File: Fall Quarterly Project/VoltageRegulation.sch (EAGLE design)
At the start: 19 parts

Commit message: Update 1.2
Introduced part of the voltage sense circuitry, filter, and amplifier. most parts still need values though, those of you with r or c values can feel free to label them.
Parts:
- removed C2: (no value), rcl:C-US050-055X075
- removed D2: (no value), diode:DIODE-DO07
- removed IC1: (no value), v-reg:78XXS
- removed VIN: (no value), con-wago-500:W237-102
- added IC3: L272M, linear:L272M
- added R1: 30k, rcl:R-US_0207/7
- added R2, R3: 10k, rcl:R-US_0207/7
- added R4: (no value), rcl:R-US_0411/12
- C1: device rcl:C-US050-055X075 -> rcl:C-US050-024X044
- D1: value (none) -> SB320; device diode:DIODE-DO07 -> diode:SB320
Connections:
- new net N$2: IC3A.OUT, IC3B.+IN, R1.2, R4.1
- new net N$4: IC3A.-IN, R1.1, R2.1
- new net N$5: C1.1, IC3A.+IN, R3.2
- new net N$6: IC3B.-IN, R4.2
- net +12V: now also IC3P.V+; no longer C1.1, D2.C, IC1.IN
- net +5V: no longer C2.1, IC1.OUT
- net 10SDIGIT5: now also U$1.D12; no longer U$1.D11
- net GND: now also IC3P.GND, R2.2; no longer C2.2, IC1.GND, VIN-2.KL
- net N$1: now also R3.1, U$1.D11; no longer D1.A, VIN-1.KL
- net N$3: now also D1.A; no longer D2.A

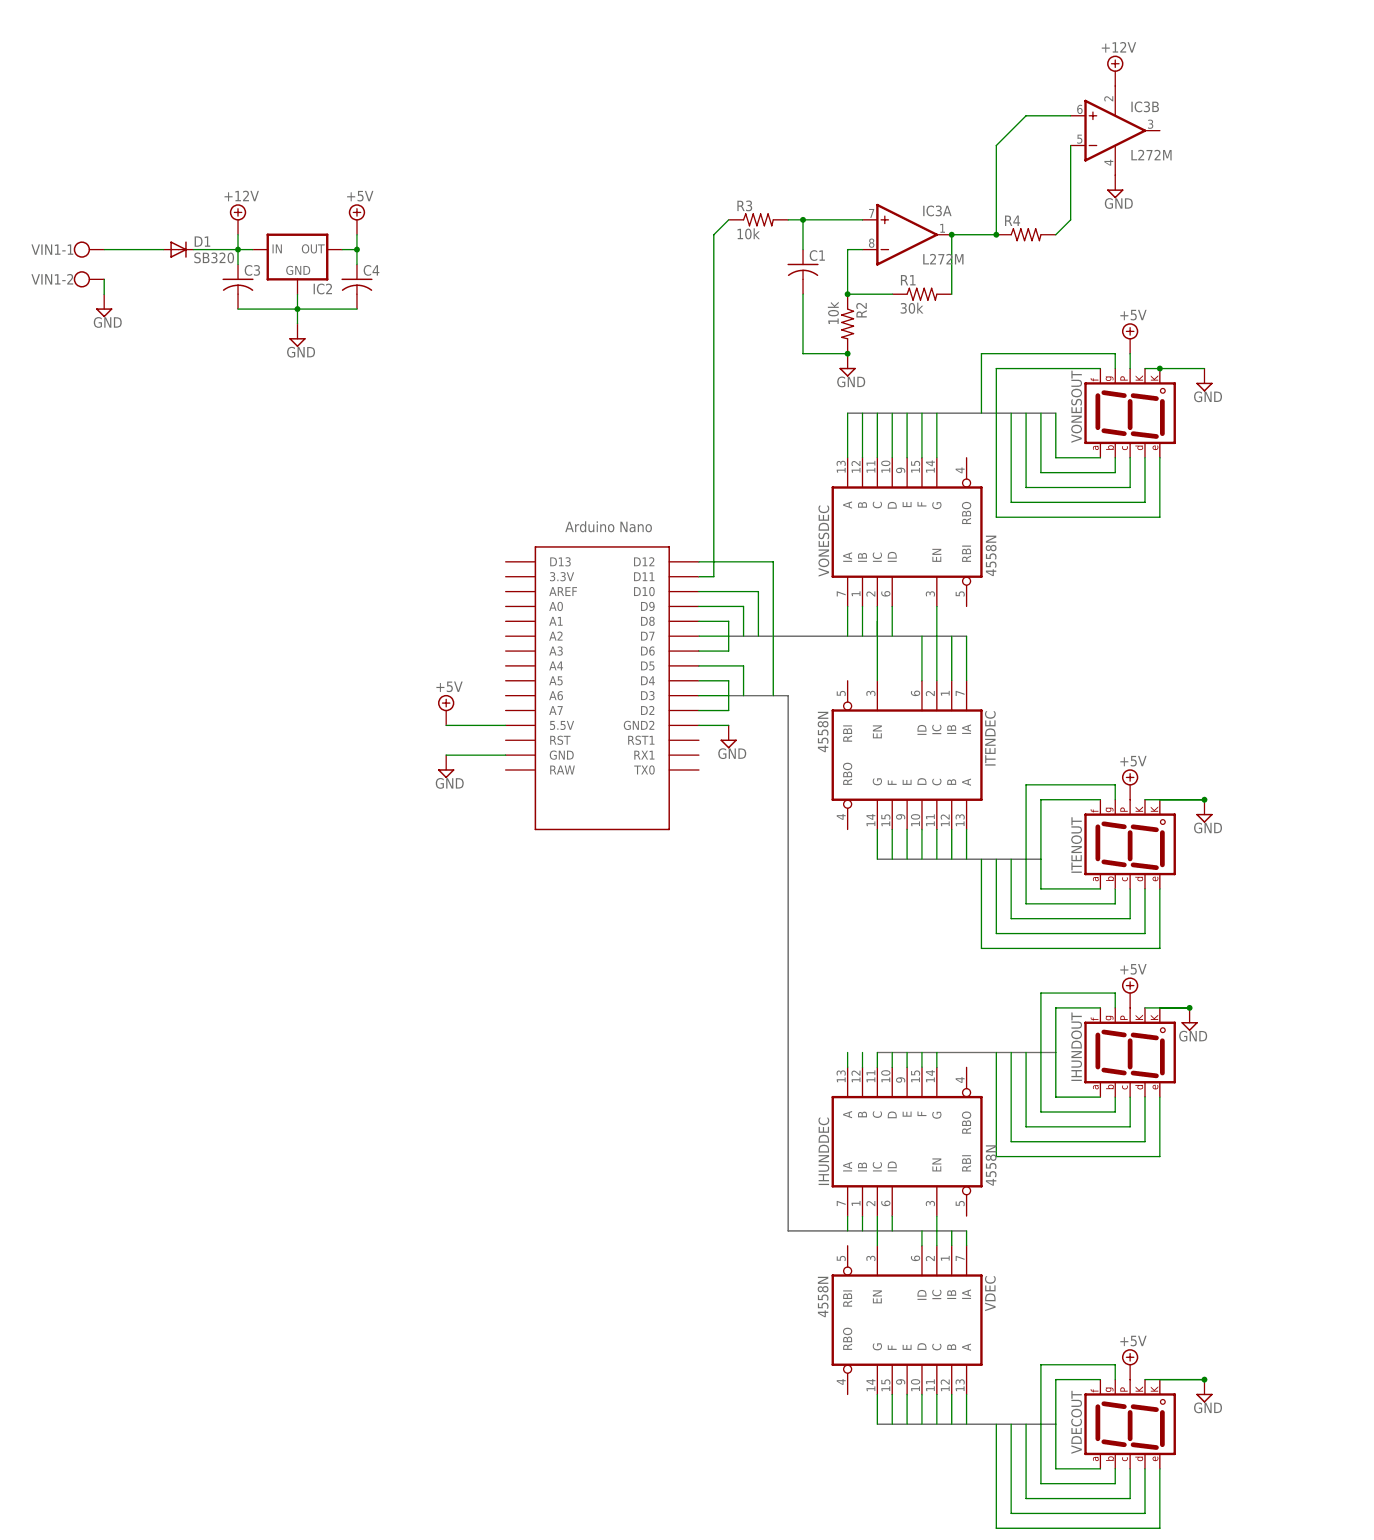
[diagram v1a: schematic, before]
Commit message: Update 1.3
All major parts have now been included in the schematic, only adjustments need to be made now. I know some resistor values have been implemented with series or parallel combinations in order use stockroom parts, and this is not accounted for. Values still need to be added to parts for the bill of materials as well as the silkscreening process. I've tried laying some traces as well in the board layout, but the config i've been trying out seems bad and needs an entire rework. We are at the point that board layout and tracing can commence.
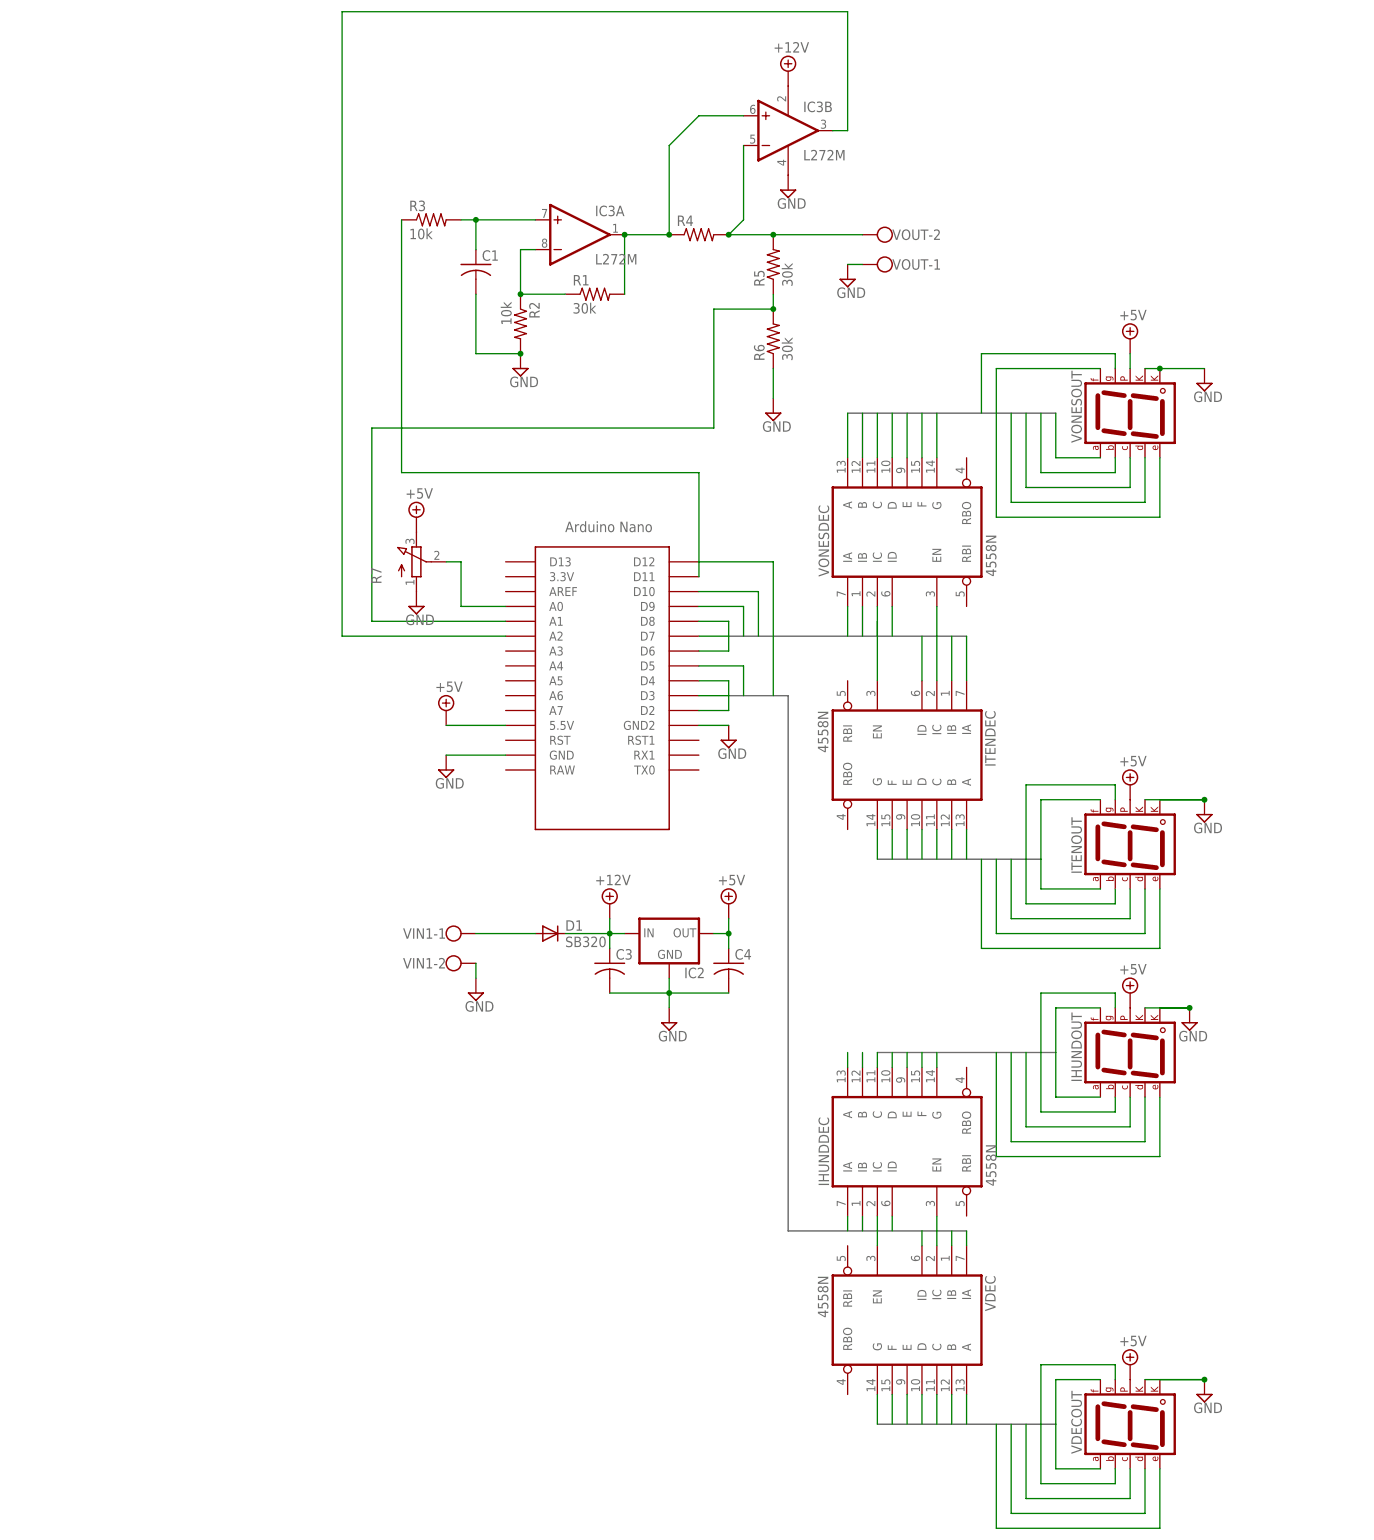
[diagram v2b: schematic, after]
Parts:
- added R5, R6: 30k, rcl:R-US_0207/7
- added R7: (no value), pot:3RP/1610N
- added VOUT: (no value), con-wago-500:W237-102
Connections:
- new net N$10: IC3B.OUT, U$1.A2
- new net N$7: R5.1, R6.2, U$1.A1
- new net N$9: R7.S, U$1.A0
- net +5V: now also R7.E
- net GND: now also R6.1, R7.A, VOUT-1.KL
- net N$6: now also R5.2, VOUT-2.KL
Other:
- moved on the sheet: C1, C3, C4, D1, IC2, IC3A, IC3B, R1, R2, R3, R4, VIN1-1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

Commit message: Update 1.4
Just began routing the board and deciding where parts will lie. I'm keeping to one layer of the board for now, that way any nets that need to be escaped to another side of the board won't need any crazy routing to reach their destination.
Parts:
- removed D1: SB320, diode:SB320
- added D2: 1N4004, diode:1N4004
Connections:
- net +12V: now also D2.C; no longer D1.C
- net +5V: now also IHUNDDECP.VSS, ITENDECP.VSS, VDECP.VSS, VONESDECP.VSS
- net 10SDIGIT5: no longer ITENDECA.EN
- net 1SDIGIT5: now also ITENDECA.EN
- net GND: now also IHUNDDECP.VDD, ITENDECP.VDD, VDECP.VDD, VONESDECP.VDD
- net N$3: now also D2.A; no longer D1.A
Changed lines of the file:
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@@
 <part name="R3" library="rcl" library_urn="urn:adsk.eagle:library:334" deviceset="R-US_" device="0207/7" package3d_urn="urn:adsk.eagle:package:23493/1" value="10k"/>
 <part name="C1" library="rcl" library_urn="urn:adsk.eagle:library:334" deviceset="C-US" device="050-024X044" package3d_urn="urn:adsk.eagle:package:23643/1"/>
-<part name="D1" library="diode" library_urn="urn:adsk.eagle:library:210" deviceset="SB320" device="" package3d_urn="urn:adsk.eagle:package:43365/1"/>
 <part name="R4" library="rcl" library_urn="urn:adsk.eagle:library:334" deviceset="R-US_" device="0411/12" package3d_urn="urn:adsk.eagle:package:23578/1"/>
 <part name="R5" library="rcl" library_urn="urn:adsk.eagle:library:334" deviceset="R-US_" device="0207/7" package3d_urn="urn:adsk.eagle:package:23493/1" value="30k">
@@
 <part name="VOUT" library="con-wago-500" library_urn="urn:adsk.eagle:library:195" deviceset="W237-102" device="" package3d_urn="urn:adsk.eagle:package:10688/1"/>
 <part name="SUPPLY22" library="supply2" library_urn="urn:adsk.eagle:library:372" deviceset="GND" device=""/>
+<part name="SUPPLY23" library="supply2" library_urn="urn:adsk.eagle:library:372" deviceset="+5V" device=""/>
+<part name="SUPPLY24" library="supply2" library_urn="urn:adsk.eagle:library:372" deviceset="+5V" device=""/>
+<part name="SUPPLY25" library="supply2" library_urn="urn:adsk.eagle:library:372" deviceset="+5V" device=""/>
+<part name="SUPPLY26" library="supply2" library_urn="urn:adsk.eagle:library:372" deviceset="+5V" device=""/>
+<part name="SUPPLY27" library="supply2" library_urn="urn:adsk.eagle:library:372" deviceset="GND" device=""/>
+<part name="SUPPLY28" library="supply2" library_urn="urn:adsk.eagle:library:372" deviceset="GND" device=""/>
+<part name="SUPPLY29" library="supply2" library_urn="urn:adsk.eagle:library:372" deviceset="GND" device=""/>
+<part name="SUPPLY30" library="supply2" library_urn="urn:adsk.eagle:library:372" deviceset="GND" device=""/>
+<part name="D2" library="diode" library_urn="urn:adsk.eagle:library:210" deviceset="1N4004" device="" package3d_urn="urn:adsk.eagle:package:43336/1"/>
 </parts>
 <sheets>
@@
 <instance part="R3" gate="G$1" x="-78.74" y="170.18"/>
 <instance part="C1" gate="G$1" x="-71.12" y="162.56"/>
-<instance part="D1" gate="1" x="-58.42" y="48.26"/>
 <instance part="R4" gate="G$1" x="-33.02" y="167.64"/>
 <instance part="R5" gate="G$1" x="-20.32" y="162.56" rot="R90">
@@
 <attribute name="R" x="-20.32" y="149.86" size="1.778" layer="96" rot="R90" display="off"/>
 </instance>
-<instance part="SUPPLY5" gate="GND" x="-20.32" y="137.16"/>
+<instance part="SUPPLY5" gate="GND" x="-20.32" y="142.24"/>
 <instance part="R7" gate="G$1" x="-81.28" y="111.76"/>
 <instance part="SUPPLY20" gate="+5V" x="-81.28" y="119.38"/>
@@
 <instance part="VOUT" gate="-2" x="0" y="167.64" rot="R180"/>
 <instance part="SUPPLY22" gate="GND" x="-7.62" y="160.02"/>
+<instance part="VONESDEC" gate="P" x="50.8" y="101.6" rot="R180"/>
+<instance part="ITENDEC" gate="P" x="76.2" y="101.6" rot="R180"/>
+<instance part="IHUNDDEC" gate="P" x="58.42" y="101.6" rot="R180"/>
+<instance part="VDEC" gate="P" x="68.58" y="101.6" rot="R180"/>
+<instance part="SUPPLY23" gate="+5V" x="58.42" y="114.3"/>
+<instance part="SUPPLY24" gate="+5V" x="50.8" y="114.3"/>
+<instance part="SUPPLY25" gate="+5V" x="68.58" y="114.3"/>
+<instance part="SUPPLY26" gate="+5V" x="76.2" y="114.3"/>
+<instance part="SUPPLY27" gate="GND" x="50.8" y="88.9"/>
+<instance part="SUPPLY28" gate="GND" x="58.42" y="88.9"/>
+<instance part="SUPPLY29" gate="GND" x="68.58" y="88.9"/>
+<instance part="SUPPLY30" gate="GND" x="76.2" y="88.9"/>
+<instance part="D2" gate="1" x="-58.42" y="48.26"/>
 </instances>
 <busses>
@@
 <bus name="4DIGIT[1..7]">
 <segment>
-<wire x1="27.94" y1="27.94" x2="-2.54" y2="27.94" width="0.762" layer="92"/>
+<wire x1="27.94" y1="27.94" x2="-7.62" y2="27.94" width="0.762" layer="92"/>
 </segment>
 </bus>
@@
 <net name="1SDIGIT3" class="0">
 <segment>
-<pinref part="VONESDEC" gate="A" pin="IC"/>
-<wire x1="-2.54" y1="99.06" x2="-2.54" y2="104.14" width="0.1524" layer="91"/>
-</segment>
-<segment>
 <pinref part="ITENDEC" gate="A" pin="IC"/>
 <wire x1="7.62" y1="99.06" x2="7.62" y2="91.44" width="0.1524" layer="91"/>
@@
 <pinref part="U$1" gate="G$1" pin="D8"/>
 <wire x1="-27.94" y1="101.6" x2="-33.02" y2="101.6" width="0.1524" layer="91"/>
+</segment>
+<segment>
+<pinref part="VONESDEC" gate="A" pin="IC"/>
+<wire x1="-2.54" y1="104.14" x2="-2.54" y2="99.06" width="0.1524" layer="91"/>
 </segment>
 </net>
@@
 <net name="4DIGIT1" class="0">
 <segment>
-<pinref part="IHUNDDEC" gate="A" pin="A"/>
-<wire x1="-7.62" y1="25.4" x2="-7.62" y2="27.94" width="0.1524" layer="91"/>
-</segment>
-<segment>
 <pinref part="IHUNDOUT" gate="G$1" pin="A"/>
 <wire x1="27.94" y1="20.32" x2="35.56" y2="20.32" width="0.1524" layer="91"/>
 <wire x1="27.94" y1="20.32" x2="27.94" y2="27.94" width="0.1524" layer="91"/>
 </segment>
+<segment>
+<pinref part="IHUNDDEC" gate="A" pin="A"/>
+<wire x1="-7.62" y1="27.94" x2="-7.62" y2="25.4" width="0.1524" layer="91"/>
+</segment>
 </net>
 <net name="4DIGIT2" class="0">
-<segment>
-<pinref part="IHUNDDEC" gate="A" pin="B"/>
-<wire x1="-5.08" y1="25.4" x2="-5.08" y2="27.94" width="0.1524" layer="91"/>
-</segment>
 <segment>
 <pinref part="IHUNDOUT" gate="G$1" pin="B"/>
@@
 <wire x1="38.1" y1="17.78" x2="25.4" y2="17.78" width="0.1524" layer="91"/>
 <wire x1="25.4" y1="17.78" x2="25.4" y2="27.94" width="0.1524" layer="91"/>
+</segment>
+<segment>
+<pinref part="IHUNDDEC" gate="A" pin="B"/>
+<wire x1="-5.08" y1="27.94" x2="-5.08" y2="25.4" width="0.1524" layer="91"/>
 </segment>
 </net>
@@
 <pinref part="SUPPLY20" gate="+5V" pin="+5V"/>
 <pinref part="R7" gate="G$1" pin="E"/>
+</segment>
+<segment>
+<pinref part="VONESDEC" gate="P" pin="VSS"/>
+<pinref part="SUPPLY24" gate="+5V" pin="+5V"/>
+<wire x1="50.8" y1="109.22" x2="50.8" y2="111.76" width="0.1524" layer="91"/>
+</segment>
+<segment>
+<pinref part="IHUNDDEC" gate="P" pin="VSS"/>
+<pinref part="SUPPLY23" gate="+5V" pin="+5V"/>
+<wire x1="58.42" y1="109.22" x2="58.42" y2="111.76" width="0.1524" layer="91"/>
+</segment>
+<segment>
+<pinref part="SUPPLY25" gate="+5V" pin="+5V"/>
+<pinref part="VDEC" gate="P" pin="VSS"/>
+<wire x1="68.58" y1="111.76" x2="68.58" y2="109.22" width="0.1524" layer="91"/>
+</segment>
+<segment>
+<pinref part="ITENDEC" gate="P" pin="VSS"/>
+<pinref part="SUPPLY26" gate="+5V" pin="+5V"/>
+<wire x1="76.2" y1="109.22" x2="76.2" y2="111.76" width="0.1524" layer="91"/>
 </segment>
 </net>
@@
 <pinref part="SUPPLY5" gate="GND" pin="GND"/>
 <pinref part="R6" gate="G$1" pin="1"/>
-<wire x1="-20.32" y1="139.7" x2="-20.32" y2="144.78" width="0.1524" layer="91"/>
 </segment>
 <segment>
@@
 <wire x1="-5.08" y1="162.56" x2="-7.62" y2="162.56" width="0.1524" layer="91"/>
 </segment>
+<segment>
+<pinref part="VONESDEC" gate="P" pin="VDD"/>
+<pinref part="SUPPLY27" gate="GND" pin="GND"/>
+<wire x1="50.8" y1="93.98" x2="50.8" y2="91.44" width="0.1524" layer="91"/>
+</segment>
+<segment>
+<pinref part="SUPPLY28" gate="GND" pin="GND"/>
+<pinref part="IHUNDDEC" gate="P" pin="VDD"/>
+<wire x1="58.42" y1="91.44" x2="58.42" y2="93.98" width="0.1524" layer="91"/>
+</segment>
+<segment>
+<pinref part="SUPPLY29" gate="GND" pin="GND"/>
+<pinref part="VDEC" gate="P" pin="VDD"/>
+<wire x1="68.58" y1="91.44" x2="68.58" y2="93.98" width="0.1524" layer="91"/>
+</segment>
+<segment>
+<pinref part="SUPPLY30" gate="GND" pin="GND"/>
+<pinref part="ITENDEC" gate="P" pin="VDD"/>
+<wire x1="76.2" y1="91.44" x2="76.2" y2="93.98" width="0.1524" layer="91"/>
+</segment>
 </net>
 <net name="1SDIGIT5" class="0">
@@
 <wire x1="-22.86" y1="99.06" x2="-22.86" y2="106.68" width="0.1524" layer="91"/>
 </segment>
+<segment>
+<pinref part="ITENDEC" gate="A" pin="EN"/>
+<wire x1="-2.54" y1="91.44" x2="-2.54" y2="99.06" width="0.1524" layer="91"/>
+</segment>
 </net>
 <net name="10SDIGIT5" class="0">
@@
 <pinref part="VDEC" gate="A" pin="EN"/>
 <wire x1="-2.54" y1="-2.54" x2="-2.54" y2="-5.08" width="0.1524" layer="91"/>
-</segment>
-<segment>
-<pinref part="ITENDEC" gate="A" pin="EN"/>
-<wire x1="-2.54" y1="101.6" x2="-2.54" y2="91.44" width="0.1524" layer="91"/>
 </segment>
 <segment>
@@
 <segment>
 <pinref part="VIN1" gate="-1" pin="KL"/>
-<pinref part="D1" gate="1" pin="A"/>
 <wire x1="-60.96" y1="48.26" x2="-71.12" y2="48.26" width="0.1524" layer="91"/>
+<pinref part="D2" gate="1" pin="A"/>
 </segment>
 </net>
@@
 <pinref part="SUPPLY18" gate="+12V" pin="+12V"/>
 <wire x1="-48.26" y1="50.8" x2="-48.26" y2="48.26" width="0.1524" layer="91"/>
-<pinref part="D1" gate="1" pin="C"/>
-</segment>
-<segment>
+<pinref part="D2" gate="1" pin="C"/>
+</segment>
+<segment>
